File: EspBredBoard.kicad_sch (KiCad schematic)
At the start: 29 parts, among them J1 USB_C_Receptacle_USB2.0, J2 USB_C_Receptacle_USB2.0, J3 Conn_01x17, J4 Conn_01x17, SW1 TS-1145A-B-A, SW2 TS-1145A-B-A, U1 CH343P, U2 ESP32-S2-WROOM-I(4M), U3 ME6217C33M5G

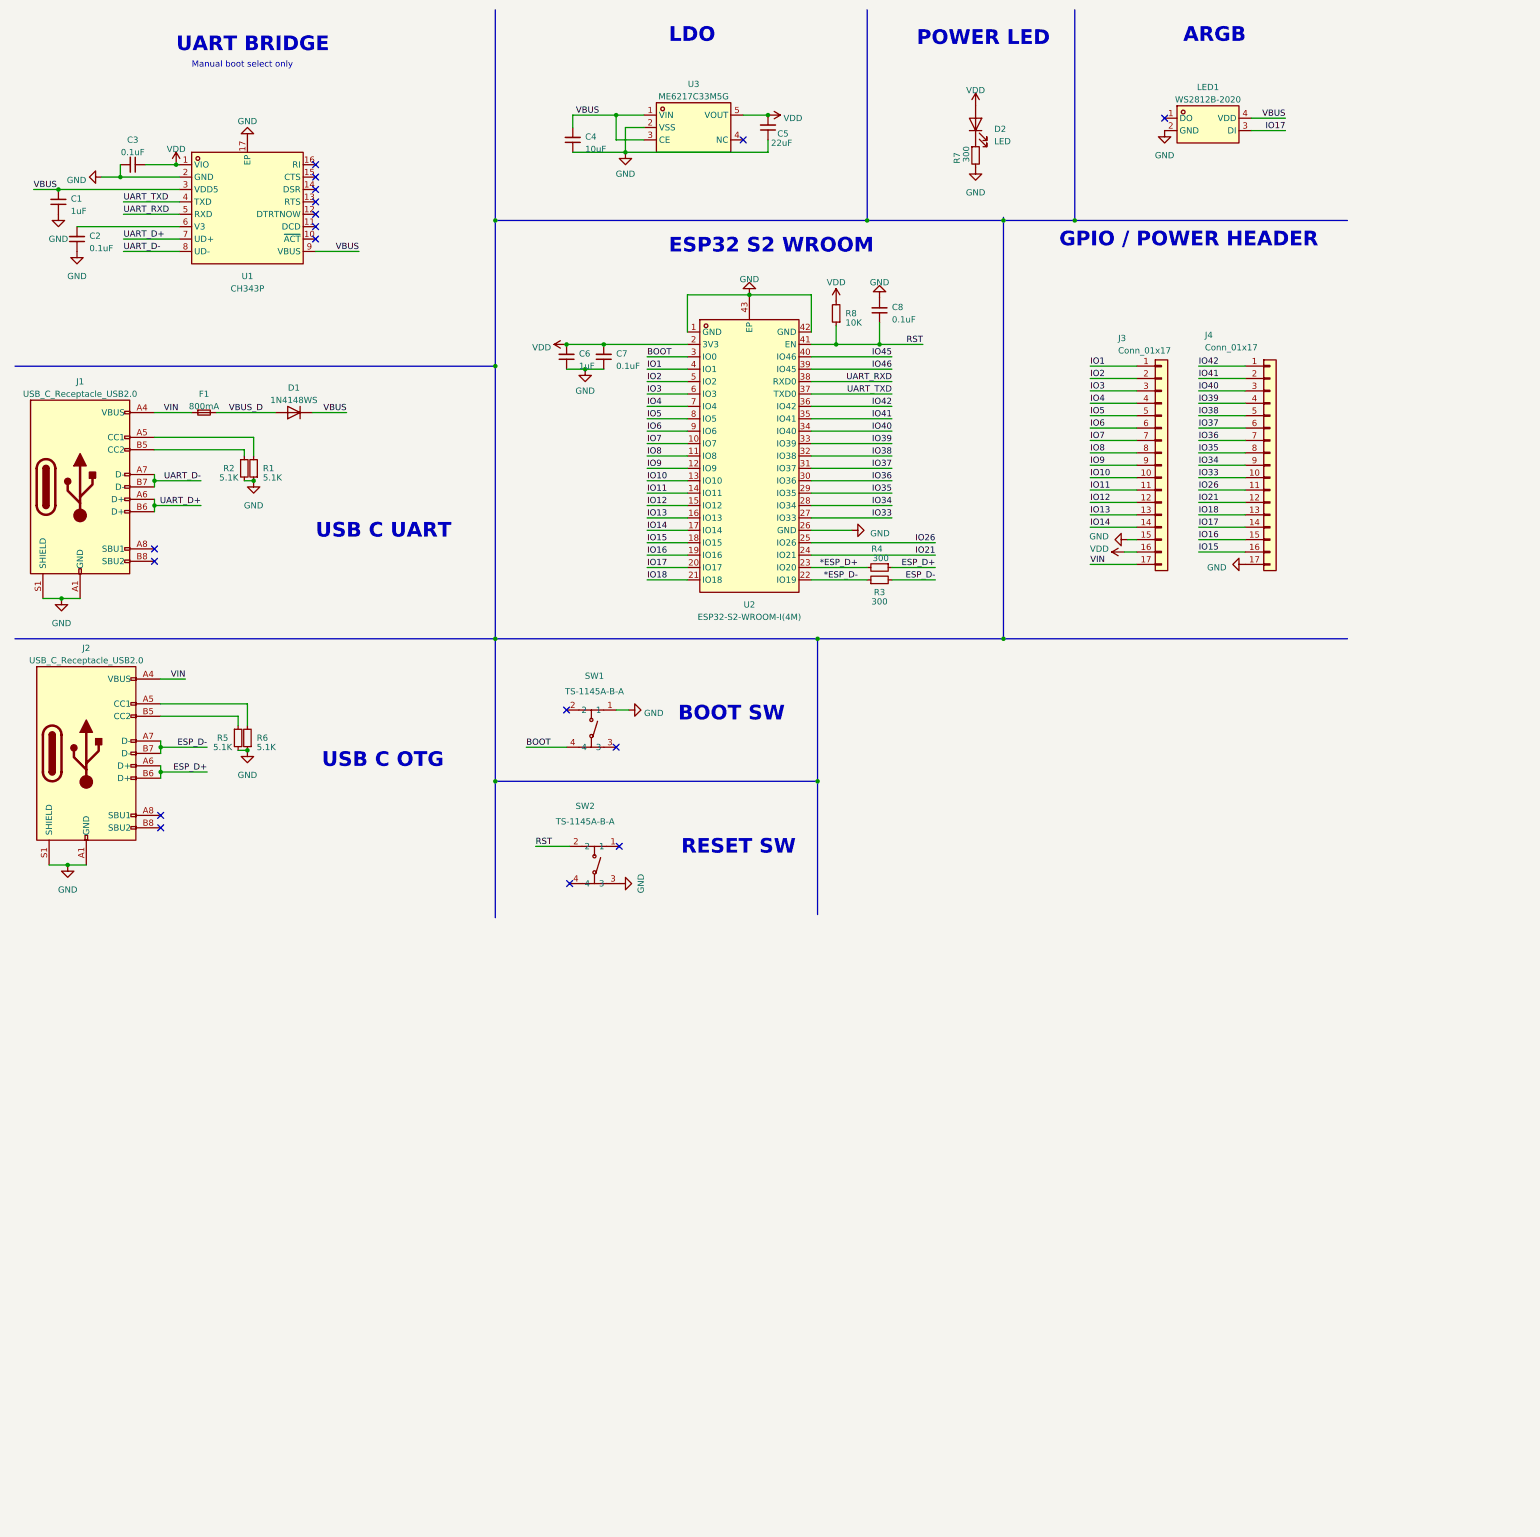
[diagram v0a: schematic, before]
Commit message: fix wrong uart route - add uart test point - add vin led
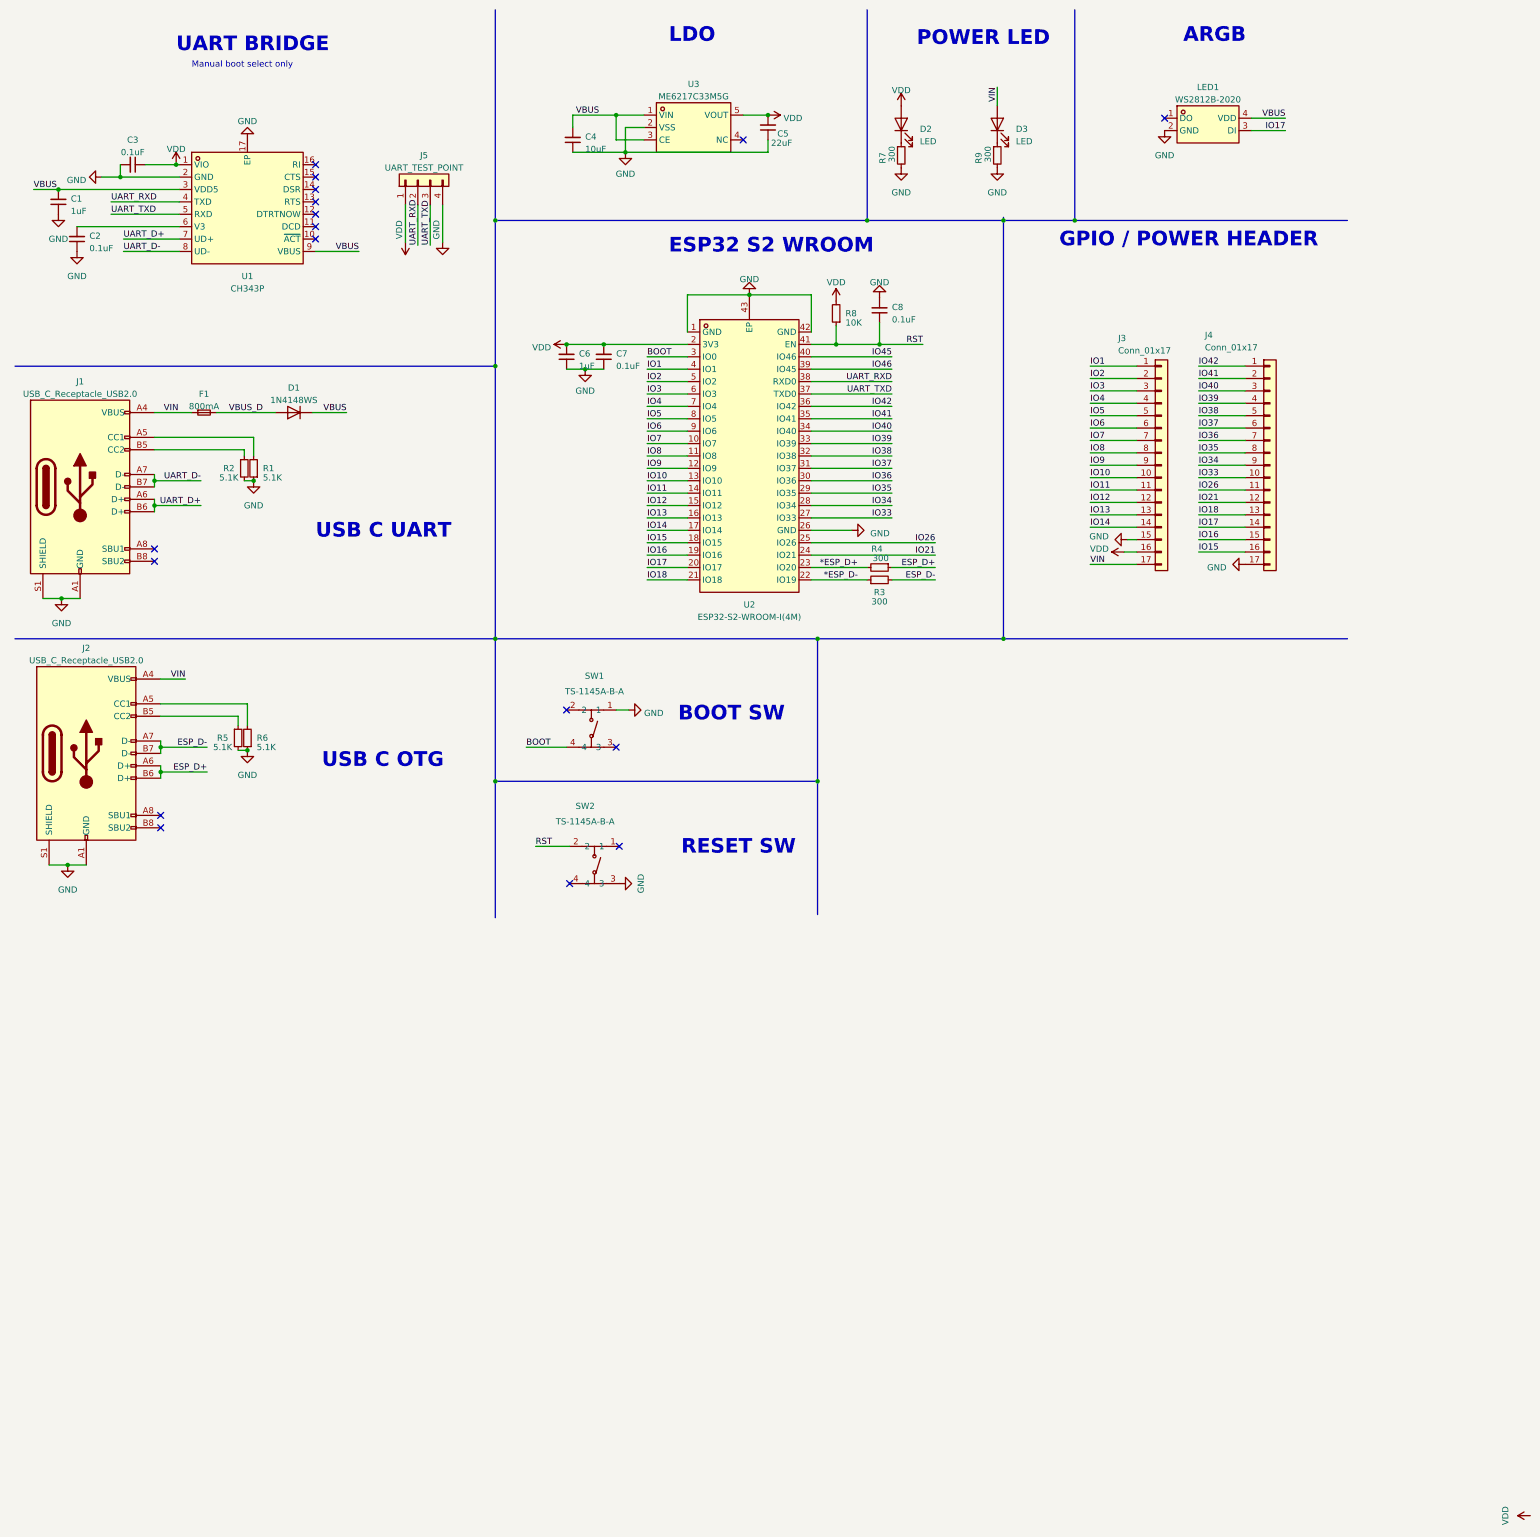
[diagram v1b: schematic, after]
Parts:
- added D3: LED, LED_SMD:LED_0603_1608Metric_Pad1.05x0.95mm_HandSolder, symbol Library:LED
- added J5: UART_TEST_POINT, Connector_PinHeader_2.54mm:PinHeader_1x04_P2.54mm_Vertical, symbol Connector_Generic:Conn_01x04
- added R9: 300, Resistor_SMD:R_0603_1608Metric_Pad0.98x0.95mm_HandSolder, symbol Library:R_Small
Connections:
- net GND: now also J5.4 (Pin_4), R9.2
- net UART_RXD: now also U1.4 (TXD), J5.2 (Pin_2); no longer U1.5 (RXD)
- net UART_TXD: now also U1.5 (RXD), J5.3 (Pin_3); no longer U1.4 (TXD)
- net VDD: now also J5.1 (Pin_1)
- net VIN: now also D3.2 (A)
- new net: D3.1 (K), R9.1
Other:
- moved on the sheet: D2, R7
